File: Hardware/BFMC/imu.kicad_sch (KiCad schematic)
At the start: 11 parts, among them J7 IMU_DATA, J8 IMU_3V3, J9 IMU_5V

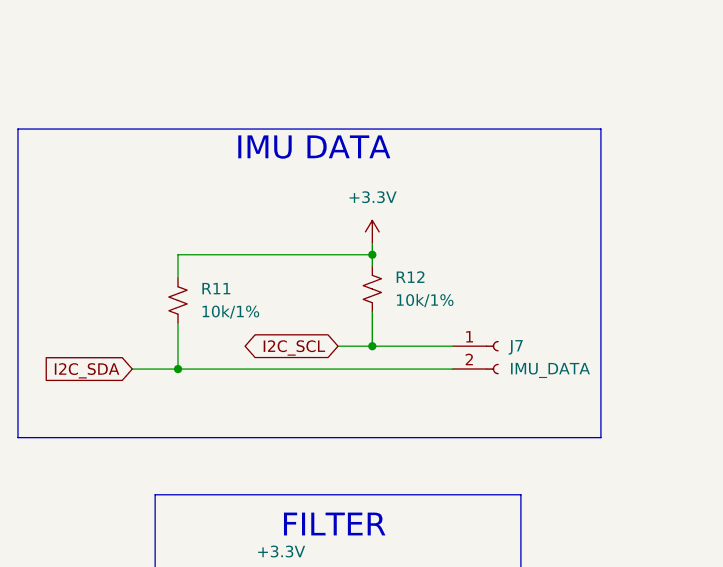
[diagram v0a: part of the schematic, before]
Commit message: update temporary file in stm32
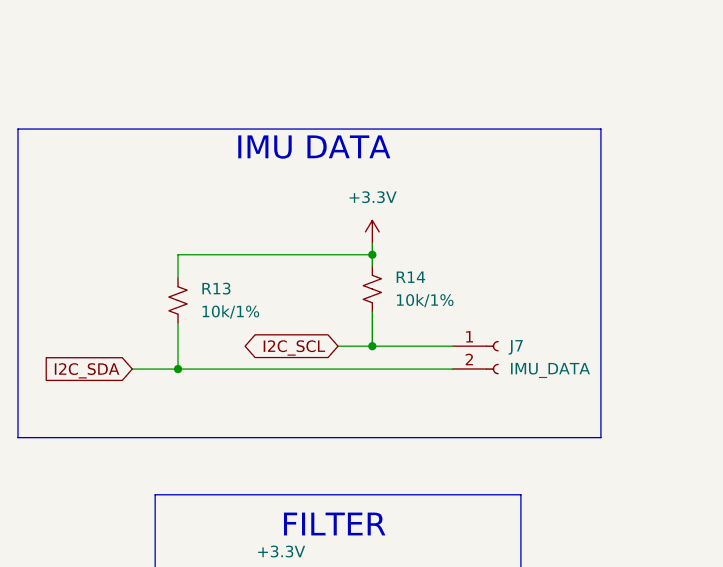
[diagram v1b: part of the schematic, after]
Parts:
- renumbered R11 to R13, R12 to R14
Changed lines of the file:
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@@
   (symbol (lib_id "Device:R_Small_US") (at 99.06 88.9 0) (unit 1)
     (in_bom yes) (on_board yes) (dnp no) (fields_autoplaced)
-    (property "Reference" "R12" (at 101.6 87.63 0)
+    (property "Reference" "R14" (at 101.6 87.63 0)
       (effects (font (size 1.27 1.27)) (justify left))
     )
@@
       (project "BFMC"
         (path "/a702f17a-d8b6-4710-aaf3-998facd86d1b/9adc05c6-e511-42a2-8bd8-d353e25d9132"
-          (reference "R12") (unit 1)
+          (reference "R14") (unit 1)
         )
       )
@@
   (symbol (lib_id "Device:R_Small_US") (at 77.47 90.17 0) (unit 1)
     (in_bom yes) (on_board yes) (dnp no) (fields_autoplaced)
-    (property "Reference" "R11" (at 80.01 88.9 0)
+    (property "Reference" "R13" (at 80.01 88.9 0)
       (effects (font (size 1.27 1.27)) (justify left))
     )
@@
       (project "BFMC"
         (path "/a702f17a-d8b6-4710-aaf3-998facd86d1b/9adc05c6-e511-42a2-8bd8-d353e25d9132"
-          (reference "R11") (unit 1)
+          (reference "R13") (unit 1)
         )
       )
